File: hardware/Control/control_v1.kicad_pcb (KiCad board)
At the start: 2 copper layers, 109.2 x 88.9 mm, 46 parts, among them J1 Conn_02x07_Counter_Clockwise, J2 Screw_Terminal_01x05, J4 RJ45, M1 STM32F4-DISCOVERY, Q1 BCX56, U1 TL2575HV-ADJ, U2 TL2575HV-ADJ, U3 DS89C21

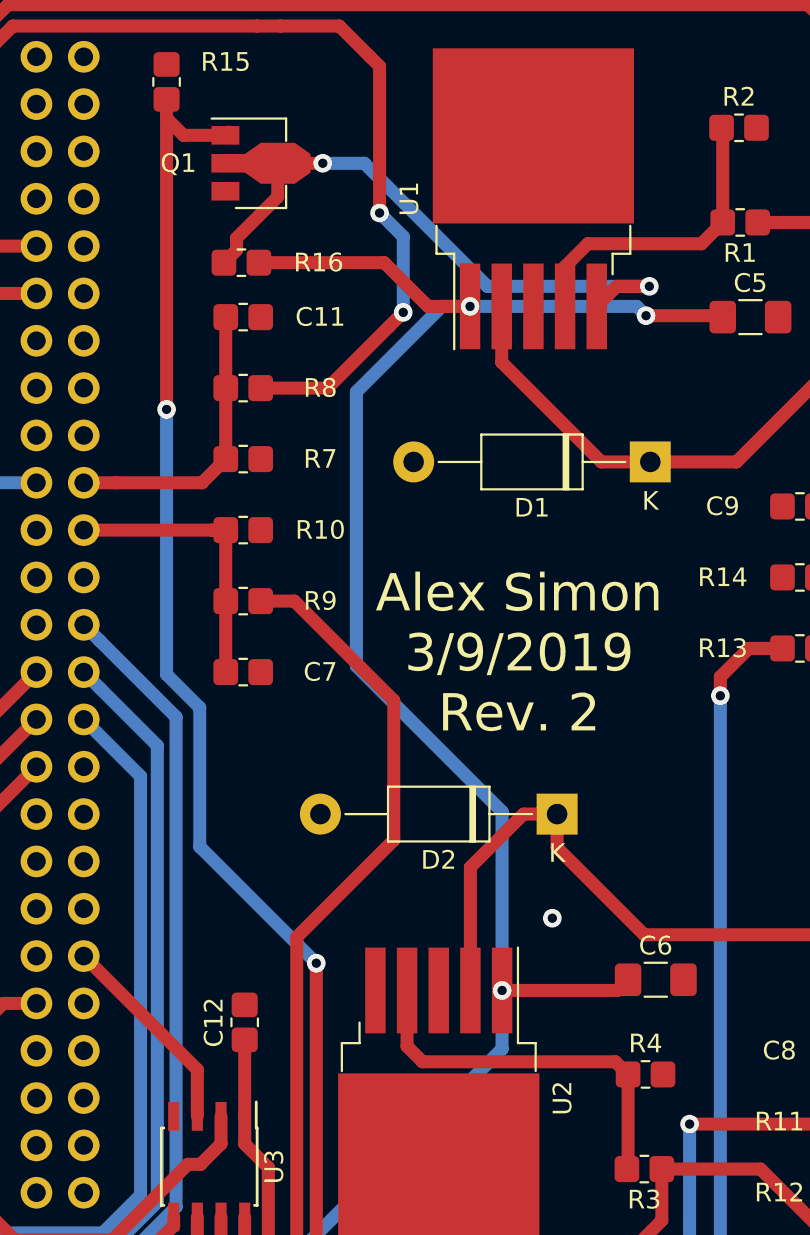
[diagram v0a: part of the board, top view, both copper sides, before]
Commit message: Addedcurrent limiting resistor, increased 2.2uF cap footprint
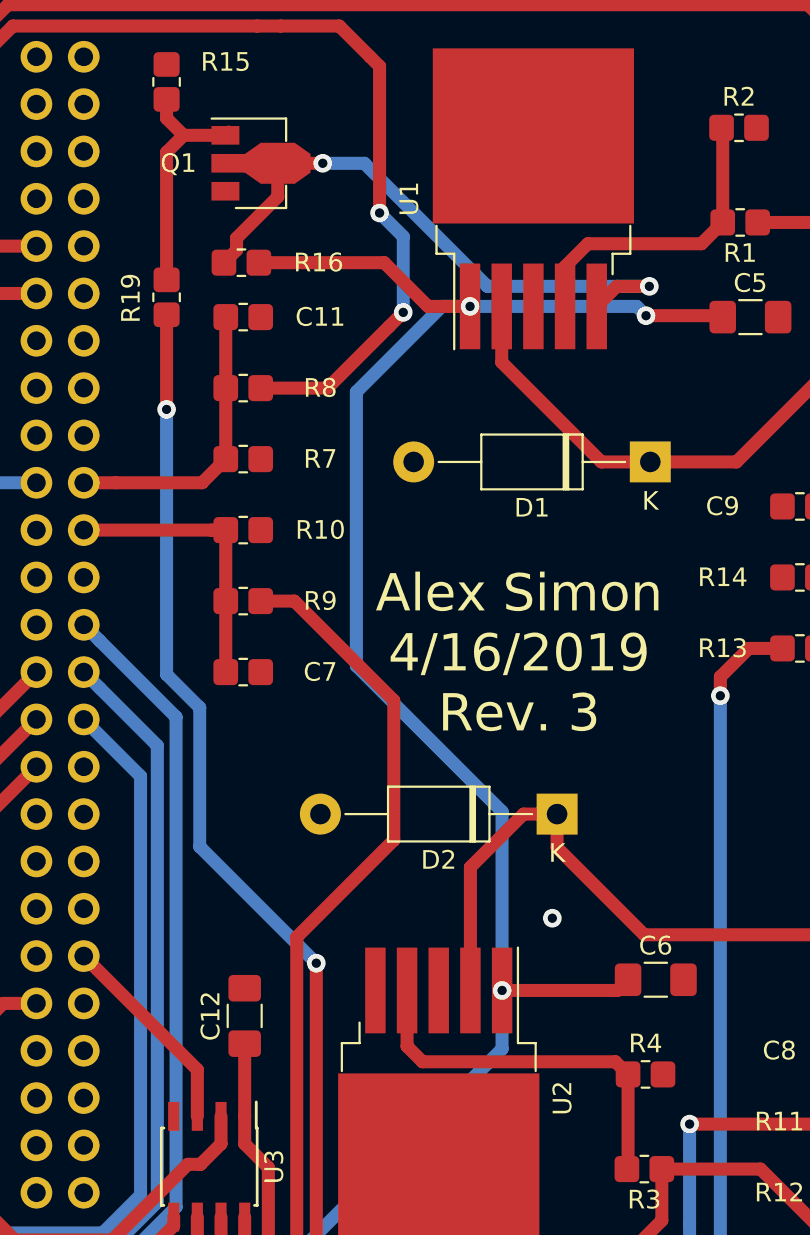
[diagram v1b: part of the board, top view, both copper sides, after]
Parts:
- added R19: 680, Resistor_SMD:R_0805_2012Metric_Pad1.33x1.40mm_HandSolder, F.Cu at (139.1, 75.1)
- C12: footprint Capacitor_SMD:C_0805_2012Metric_Pad1.33x1.40mm_HandSolder -> Capacitor_SMD:C_1206_3216Metric_Pad1.42x1.75mm_HandSolder
- moved C12 0.34 mm to (143.3, 113.7)
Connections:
- J4 pad 4: Net-(J4-Pad4) -> (no net)
- M1 pad 10: Net-(M1-Pad10) -> (no net)
- M1 pad 12: Net-(M1-Pad12) -> (no net)
- M1 pad 13: Net-(M1-Pad13) -> (no net)
- M1 pad 14: Net-(M1-Pad14) -> (no net)
- M1 pad 15: Net-(M1-Pad15) -> (no net)
- M1 pad 16: Net-(M1-Pad16) -> (no net)
- M1 pad 17: Net-(M1-Pad17) -> (no net)
- M1 pad 18: Net-(M1-Pad18) -> (no net)
- M1 pad 21: Net-(M1-Pad21) -> (no net)
- M1 pad 24: Net-(M1-Pad24) -> (no net)
- M1 pad 25: Net-(M1-Pad25) -> (no net)
- M1 pad 3: Net-(M1-Pad3) -> (no net)
- M1 pad 32: Net-(M1-Pad32) -> (no net)
- M1 pad 33: Net-(M1-Pad33) -> (no net)
- M1 pad 34: Net-(M1-Pad34) -> (no net)
- M1 pad 35: Net-(M1-Pad35) -> (no net)
- M1 pad 36: Net-(M1-Pad36) -> (no net)
- M1 pad 37: Net-(M1-Pad37) -> (no net)
- M1 pad 38: Net-(M1-Pad38) -> (no net)
- M1 pad 39: Net-(M1-Pad39) -> (no net)
- M1 pad 4: Net-(M1-Pad4) -> (no net)
- M1 pad 42: Net-(M1-Pad42) -> (no net)
- M1 pad 43: Net-(M1-Pad43) -> (no net)
- M1 pad 44: Net-(M1-Pad44) -> (no net)
- M1 pad 45: Net-(M1-Pad45) -> (no net)
- M1 pad 46: Net-(M1-Pad46) -> (no net)
- M1 pad 47: Net-(M1-Pad47) -> (no net)
- M1 pad 48: Net-(M1-Pad48) -> (no net)
- M1 pad 55: Net-(M1-Pad55) -> (no net)
- M1 pad 56: Net-(M1-Pad56) -> (no net)
- M1 pad 57: Net-(M1-Pad57) -> (no net)
- M1 pad 58: Net-(M1-Pad58) -> (no net)
- M1 pad 59: Net-(M1-Pad59) -> (no net)
- M1 pad 6: Net-(M1-Pad6) -> (no net)
- M1 pad 60: Net-(M1-Pad60) -> (no net)
- M1 pad 61: Net-(M1-Pad61) -> (no net)
- M1 pad 62: Net-(M1-Pad62) -> (no net)
- M1 pad 63: Net-(M1-Pad63) -> (no net)
- M1 pad 64: Net-(M1-Pad64) -> (no net)
- M1 pad 65: Net-(M1-Pad65) -> (no net)
- M1 pad 66: Net-(M1-Pad66) -> (no net)
- M1 pad 67: Net-(M1-Pad67) -> (no net)
- M1 pad 68: Net-(M1-Pad68) -> (no net)
- M1 pad 69: Net-(M1-Pad69) -> (no net)
- M1 pad 7: Net-(M1-Pad7) -> (no net)
- M1 pad 70: Net-(M1-Pad70) -> (no net)
- M1 pad 71: Net-(M1-Pad71) -> (no net)
- M1 pad 72: Net-(M1-Pad72) -> (no net)
- M1 pad 73: Net-(M1-Pad73) -> (no net)
- M1 pad 74: Net-(M1-Pad74) -> (no net)
- M1 pad 77: Net-(M1-Pad77) -> (no net)
- M1 pad 78: Net-(M1-Pad78) -> (no net)
- M1 pad 79: Net-(M1-Pad79) -> (no net)
- M1 pad 8: Net-(M1-Pad8) -> (no net)
- M1 pad 80: Net-(M1-Pad80) -> (no net)
- M1 pad 81: Net-(M1-Pad81) -> (no net)
- M1 pad 82: Net-(M1-Pad82) -> (no net)
- M1 pad 83: Net-(M1-Pad83) -> (no net)
- M1 pad 84: Net-(M1-Pad84) -> (no net)
- M1 pad 85: Net-(M1-Pad85) -> (no net)
- M1 pad 86: Net-(M1-Pad86) -> (no net)
- M1 pad 87: Net-(M1-Pad87) -> (no net)
- M1 pad 88: Net-(M1-Pad88) -> (no net)
- M1 pad 89: Net-(M1-Pad89) -> (no net)
- M1 pad 90: Net-(M1-Pad90) -> (no net)
- M1 pad 91: Net-(M1-Pad91) -> (no net)
- M1 pad 92: Net-(M1-Pad92) -> (no net)
- M1 pad 93: Net-(M1-Pad93) -> (no net)
- M1 pad 94: Net-(M1-Pad94) -> (no net)
- M1 pad 95: Net-(M1-Pad95) -> (no net)
- M1 pad 96: Net-(M1-Pad96) -> (no net)
- M1 pad 97: Net-(M1-Pad97) -> (no net)
- M1 pad 98: Net-(M1-Pad98) -> (no net)
- Q1 pad 1: /TransEnable_TTL -> Net-(Q1-Pad1)
- R15 pad 1: /TransEnable_TTL -> Net-(Q1-Pad1)
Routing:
- net /TransEnable_TTL: track 92.1 -> 76.6 mm
- net Net-(Q1-Pad1): track 0.00 -> 13.0 mm
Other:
- board text added: "Alex Simon 4/16/2019 Rev. 3"
- board text removed: "Alex Simon 3/9/2019 Rev. 2"

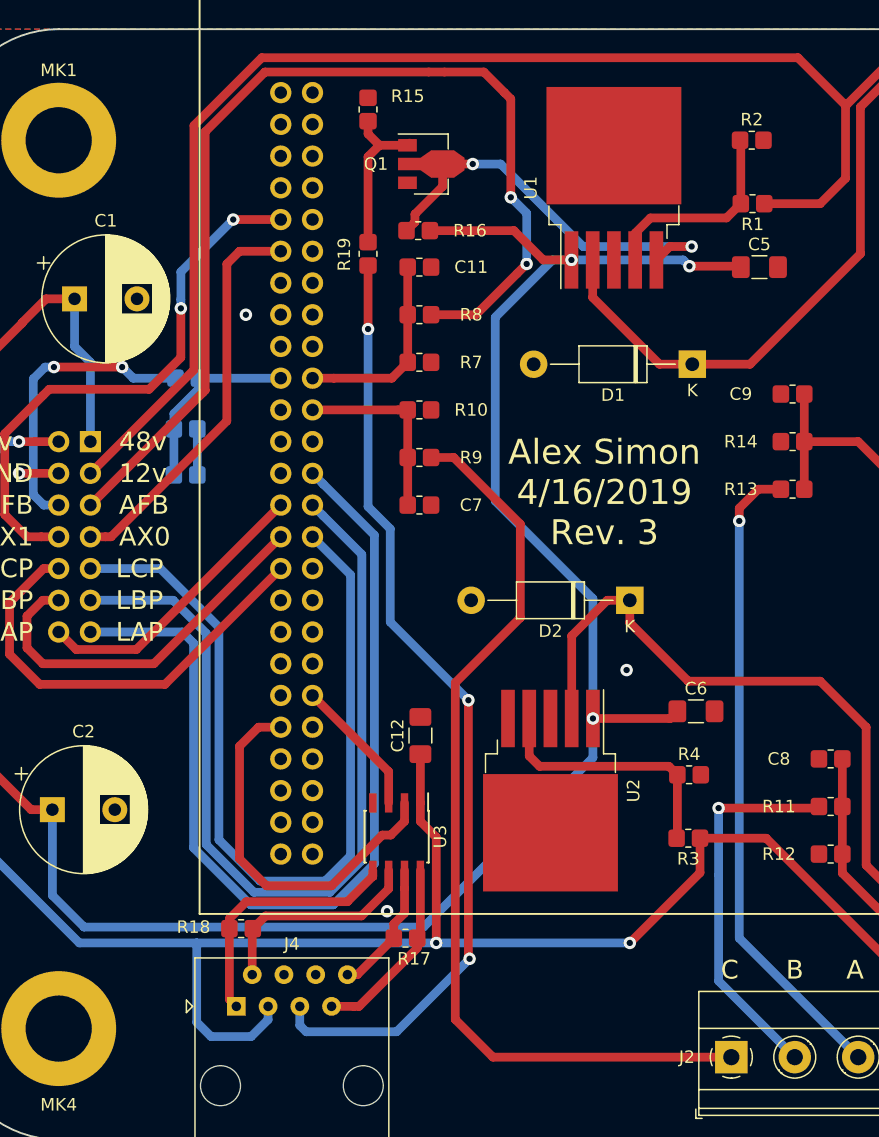
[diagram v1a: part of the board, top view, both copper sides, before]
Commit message: Added RS485 bias resistors
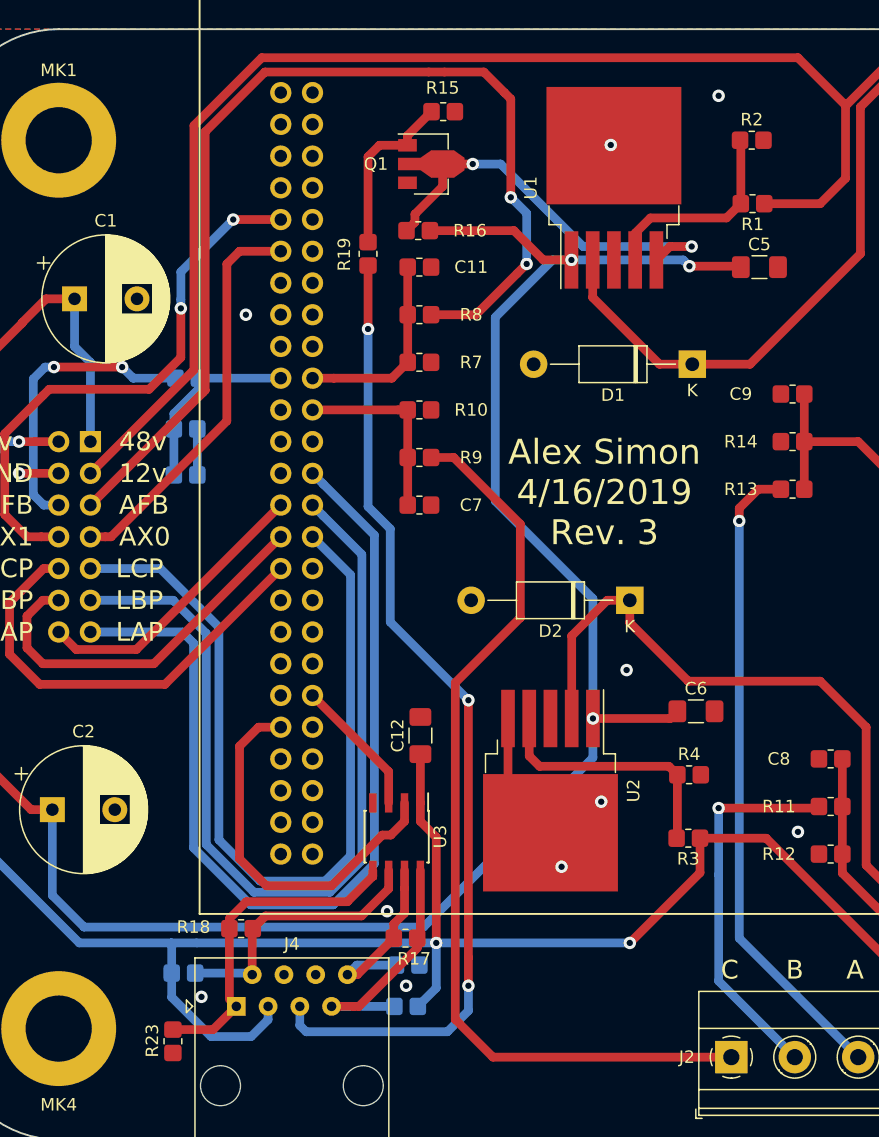
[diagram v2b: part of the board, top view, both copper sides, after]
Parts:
- added R20: 680, Resistor_SMD:R_0805_2012Metric_Pad1.33x1.40mm_HandSolder, B.Cu at (142.1, 135.4)
- added R21: 680, Resistor_SMD:R_0805_2012Metric_Pad1.33x1.40mm_HandSolder, B.Cu at (142.2, 132.1)
- added R22: 680, Resistor_SMD:R_0805_2012Metric_Pad1.33x1.40mm_HandSolder, B.Cu at (124.3, 132.7)
- added R23: 680, Resistor_SMD:R_0805_2012Metric_Pad1.33x1.40mm_HandSolder, F.Cu at (123.4, 138.2)
- moved R15 6.02 mm to (145.1, 63.8), turned to 0 degrees
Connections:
- J4 pad 4: (no net) -> Net-(J4-Pad4)
- M1 pad 10: (no net) -> Net-(M1-Pad10)
- M1 pad 12: (no net) -> Net-(M1-Pad12)
- M1 pad 13: (no net) -> Net-(M1-Pad13)
- M1 pad 14: (no net) -> Net-(M1-Pad14)
- M1 pad 15: (no net) -> Net-(M1-Pad15)
- M1 pad 16: (no net) -> Net-(M1-Pad16)
- M1 pad 17: (no net) -> Net-(M1-Pad17)
- M1 pad 18: (no net) -> Net-(M1-Pad18)
- M1 pad 21: (no net) -> Net-(M1-Pad21)
- M1 pad 24: (no net) -> Net-(M1-Pad24)
- M1 pad 25: (no net) -> Net-(M1-Pad25)
- M1 pad 3: (no net) -> Net-(M1-Pad3)
- M1 pad 32: (no net) -> Net-(M1-Pad32)
- M1 pad 33: (no net) -> Net-(M1-Pad33)
- M1 pad 34: (no net) -> Net-(M1-Pad34)
- M1 pad 35: (no net) -> Net-(M1-Pad35)
- M1 pad 36: (no net) -> Net-(M1-Pad36)
- M1 pad 37: (no net) -> Net-(M1-Pad37)
- M1 pad 38: (no net) -> Net-(M1-Pad38)
- M1 pad 39: (no net) -> Net-(M1-Pad39)
- M1 pad 4: (no net) -> Net-(M1-Pad4)
- M1 pad 42: (no net) -> Net-(M1-Pad42)
- M1 pad 43: (no net) -> Net-(M1-Pad43)
- M1 pad 44: (no net) -> Net-(M1-Pad44)
- M1 pad 45: (no net) -> Net-(M1-Pad45)
- M1 pad 46: (no net) -> Net-(M1-Pad46)
- M1 pad 47: (no net) -> Net-(M1-Pad47)
- M1 pad 48: (no net) -> Net-(M1-Pad48)
- M1 pad 55: (no net) -> Net-(M1-Pad55)
- M1 pad 56: (no net) -> Net-(M1-Pad56)
- M1 pad 57: (no net) -> Net-(M1-Pad57)
- M1 pad 58: (no net) -> Net-(M1-Pad58)
- M1 pad 59: (no net) -> Net-(M1-Pad59)
- M1 pad 6: (no net) -> Net-(M1-Pad6)
- M1 pad 60: (no net) -> Net-(M1-Pad60)
- M1 pad 61: (no net) -> Net-(M1-Pad61)
- M1 pad 62: (no net) -> Net-(M1-Pad62)
- M1 pad 63: (no net) -> Net-(M1-Pad63)
- M1 pad 64: (no net) -> Net-(M1-Pad64)
- M1 pad 65: (no net) -> Net-(M1-Pad65)
- M1 pad 66: (no net) -> Net-(M1-Pad66)
- M1 pad 67: (no net) -> Net-(M1-Pad67)
- M1 pad 68: (no net) -> Net-(M1-Pad68)
- M1 pad 69: (no net) -> Net-(M1-Pad69)
- M1 pad 7: (no net) -> Net-(M1-Pad7)
- M1 pad 70: (no net) -> Net-(M1-Pad70)
- M1 pad 71: (no net) -> Net-(M1-Pad71)
- M1 pad 72: (no net) -> Net-(M1-Pad72)
- M1 pad 73: (no net) -> Net-(M1-Pad73)
- M1 pad 74: (no net) -> Net-(M1-Pad74)
- M1 pad 77: (no net) -> Net-(M1-Pad77)
- M1 pad 78: (no net) -> Net-(M1-Pad78)
- M1 pad 79: (no net) -> Net-(M1-Pad79)
- M1 pad 8: (no net) -> Net-(M1-Pad8)
- M1 pad 80: (no net) -> Net-(M1-Pad80)
- M1 pad 81: (no net) -> Net-(M1-Pad81)
- M1 pad 82: (no net) -> Net-(M1-Pad82)
- M1 pad 83: (no net) -> Net-(M1-Pad83)
- M1 pad 84: (no net) -> Net-(M1-Pad84)
- M1 pad 85: (no net) -> Net-(M1-Pad85)
- M1 pad 86: (no net) -> Net-(M1-Pad86)
- M1 pad 87: (no net) -> Net-(M1-Pad87)
- M1 pad 88: (no net) -> Net-(M1-Pad88)
- M1 pad 89: (no net) -> Net-(M1-Pad89)
- M1 pad 90: (no net) -> Net-(M1-Pad90)
- M1 pad 91: (no net) -> Net-(M1-Pad91)
- M1 pad 92: (no net) -> Net-(M1-Pad92)
- M1 pad 93: (no net) -> Net-(M1-Pad93)
- M1 pad 94: (no net) -> Net-(M1-Pad94)
- M1 pad 95: (no net) -> Net-(M1-Pad95)
- M1 pad 96: (no net) -> Net-(M1-Pad96)
- M1 pad 97: (no net) -> Net-(M1-Pad97)
- M1 pad 98: (no net) -> Net-(M1-Pad98)
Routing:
- net /GND: track 7.19 -> 17.7 mm, vias 4 -> 11
- net /5v: track 263.0 -> 269.5 mm
- net /-TX: track 20.6 -> 25.7 mm
- net /+RX: track 15.1 -> 20.2 mm
- net /+TX: track 17.4 -> 22.0 mm
- net /-RX: track 10.7 -> 14.9 mm
- net /TransEnable_TTL: track 76.6 -> 78.9 mm
- net Net-(Q1-Pad1): track 13.0 -> 13.9 mm

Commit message: Updated Documentation
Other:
- board text added: "Alex Simon 4/27/2019 Rev. 3"
- board text removed: "Alex Simon 4/16/2019 Rev. 3"
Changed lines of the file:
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@@
     (effects (font (size 1.5 1.5) (thickness 0.3)))
   )
-  (gr_text "Alex Simon\n4/16/2019\nRev. 3" (at 157.988 94.234) (layer F.SilkS)
+  (gr_text "Alex Simon\n4/27/2019\nRev. 3" (at 157.988 94.234) (layer F.SilkS)
     (effects (font (size 2 2) (thickness 0.3)))
   )
-  (gr_text "Alex Simon\n4/16/2019\nRev. 3" (at 157.988 94.234) (layer B.SilkS)
+  (gr_text "Alex Simon\n4/27/2019\nRev. 3" (at 157.988 94.234) (layer B.SilkS)
     (effects (font (size 3 3) (thickness 0.3)) (justify mirror))
   )
@@
   (gr_line (start 205.74 57.15) (end 114.3 57.15) (layer Edge.Cuts) (width 0.15))
   (gr_line (start 214.63 137.16) (end 214.63 66.04) (layer Edge.Cuts) (width 0.15))
-  (via (at 158.496 66.421) (size 1) (drill 0.5) (layers F.Cu B.Cu) (net 2))
-  (via (at 154.559 124.206) (size 1) (drill 0.5) (layers F.Cu B.Cu) (net 2))
-  (via (at 157.734 118.999) (size 1) (drill 0.5) (layers F.Cu B.Cu) (net 2))
   (via (at 155.35 75.625) (size 1) (drill 0.5) (layers F.Cu B.Cu) (net 1) (status 30))
   (segment (start 163.255 112.335) (end 163.83 111.76) (width 0.7) (layer F.Cu) (net 1) (status 30))
@@
   (segment (start 153.095 75.625) (end 155.35 75.625) (width 0.7) (layer F.Cu) (net 1) (status 20))
   (segment (start 150.749 73.279) (end 153.095 75.625) (width 0.7) (layer F.Cu) (net 1))
+  (via (at 158.496 66.421) (size 1) (drill 0.5) (layers F.Cu B.Cu) (net 2))
+  (via (at 154.559 124.206) (size 1) (drill 0.5) (layers F.Cu B.Cu) (net 2))
+  (via (at 157.734 118.999) (size 1) (drill 0.5) (layers F.Cu B.Cu) (net 2))
   (segment (start 171.885 76.2) (end 171.885 76.527) (width 0.7) (layer F.Cu) (net 2) (status 30))
   (via (at 159.766 108.458) (size 1) (drill 0.5) (layers F.Cu B.Cu) (net 2))

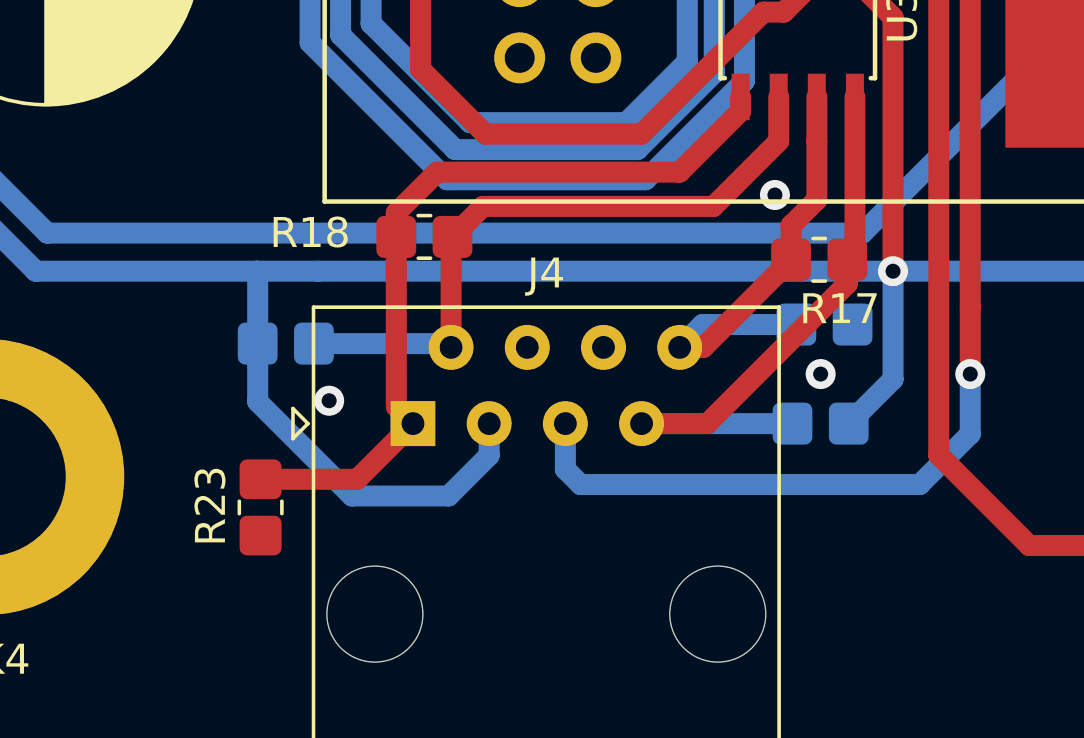
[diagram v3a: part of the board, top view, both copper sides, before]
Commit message: Removed voltage biasing resistors from control board
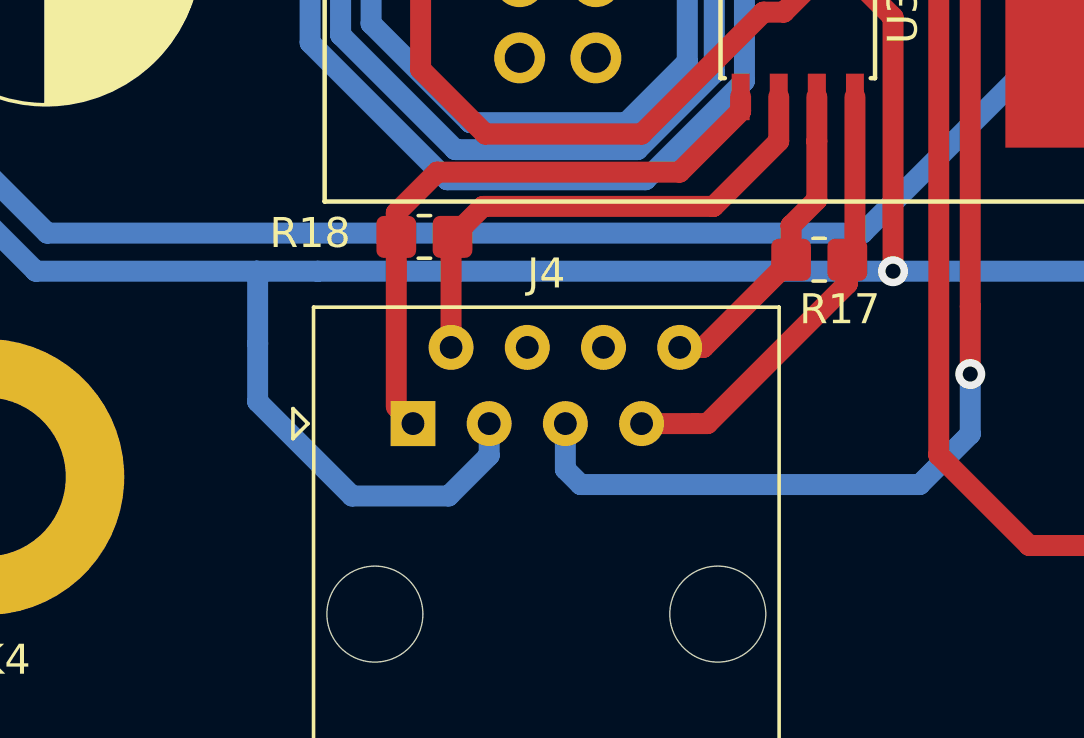
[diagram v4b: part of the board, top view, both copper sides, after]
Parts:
- removed R20, R21, R22, R23: 680, Resistor_SMD:R_0805_2012Metric_Pad1.33x1.40mm_HandSolder
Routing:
- net /-TX: track 25.7 -> 19.8 mm
- net /5v: track 269.5 -> 263.8 mm
- net /+RX: track 20.2 -> 15.1 mm
- net /+TX: track 22.0 -> 17.6 mm
- net /-RX: track 14.9 -> 10.7 mm
- net /GND: vias 11 -> 8

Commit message: Update voltage divider on 12v enable transistor
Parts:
- R15: value 2k -> 6k
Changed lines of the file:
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@@
   (title_block
     (title "Brushless DC Motor Controller")
-    (date 2019-02-12)
+    (date 2019-05-08)
     (rev 1)
     (company "Loma Incorporated")
@@
       (effects (font (size 1 1) (thickness 0.15)))
     )
-    (fp_text value 2k (at 0 1.65) (layer F.Fab)
-      (effects (font (size 1 1) (thickness 0.15)))
-    )
+    (fp_text value 6k (at 0 1.65) (layer F.Fab)
+      (effects (font (size 1 1) (thickness 0.15)))
+    )
